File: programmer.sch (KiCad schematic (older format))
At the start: 59 parts, among them U15 93LCxxBT-I_OT, U16 FT2232H, U17 SN74LVC1G32DBVR, U18 SN74LVC2T45DCUR, U19 SN74LVC2T45DCUR, U20 SN74AXC4T245PWR, U21 SN74LVC2T45DCUR, U22 SN74LVC2T45DCUR, U23 SN74LVC2G07DCKR, U24 W25Q64JV, Y2 ECS-3225S33-120-FN-TR

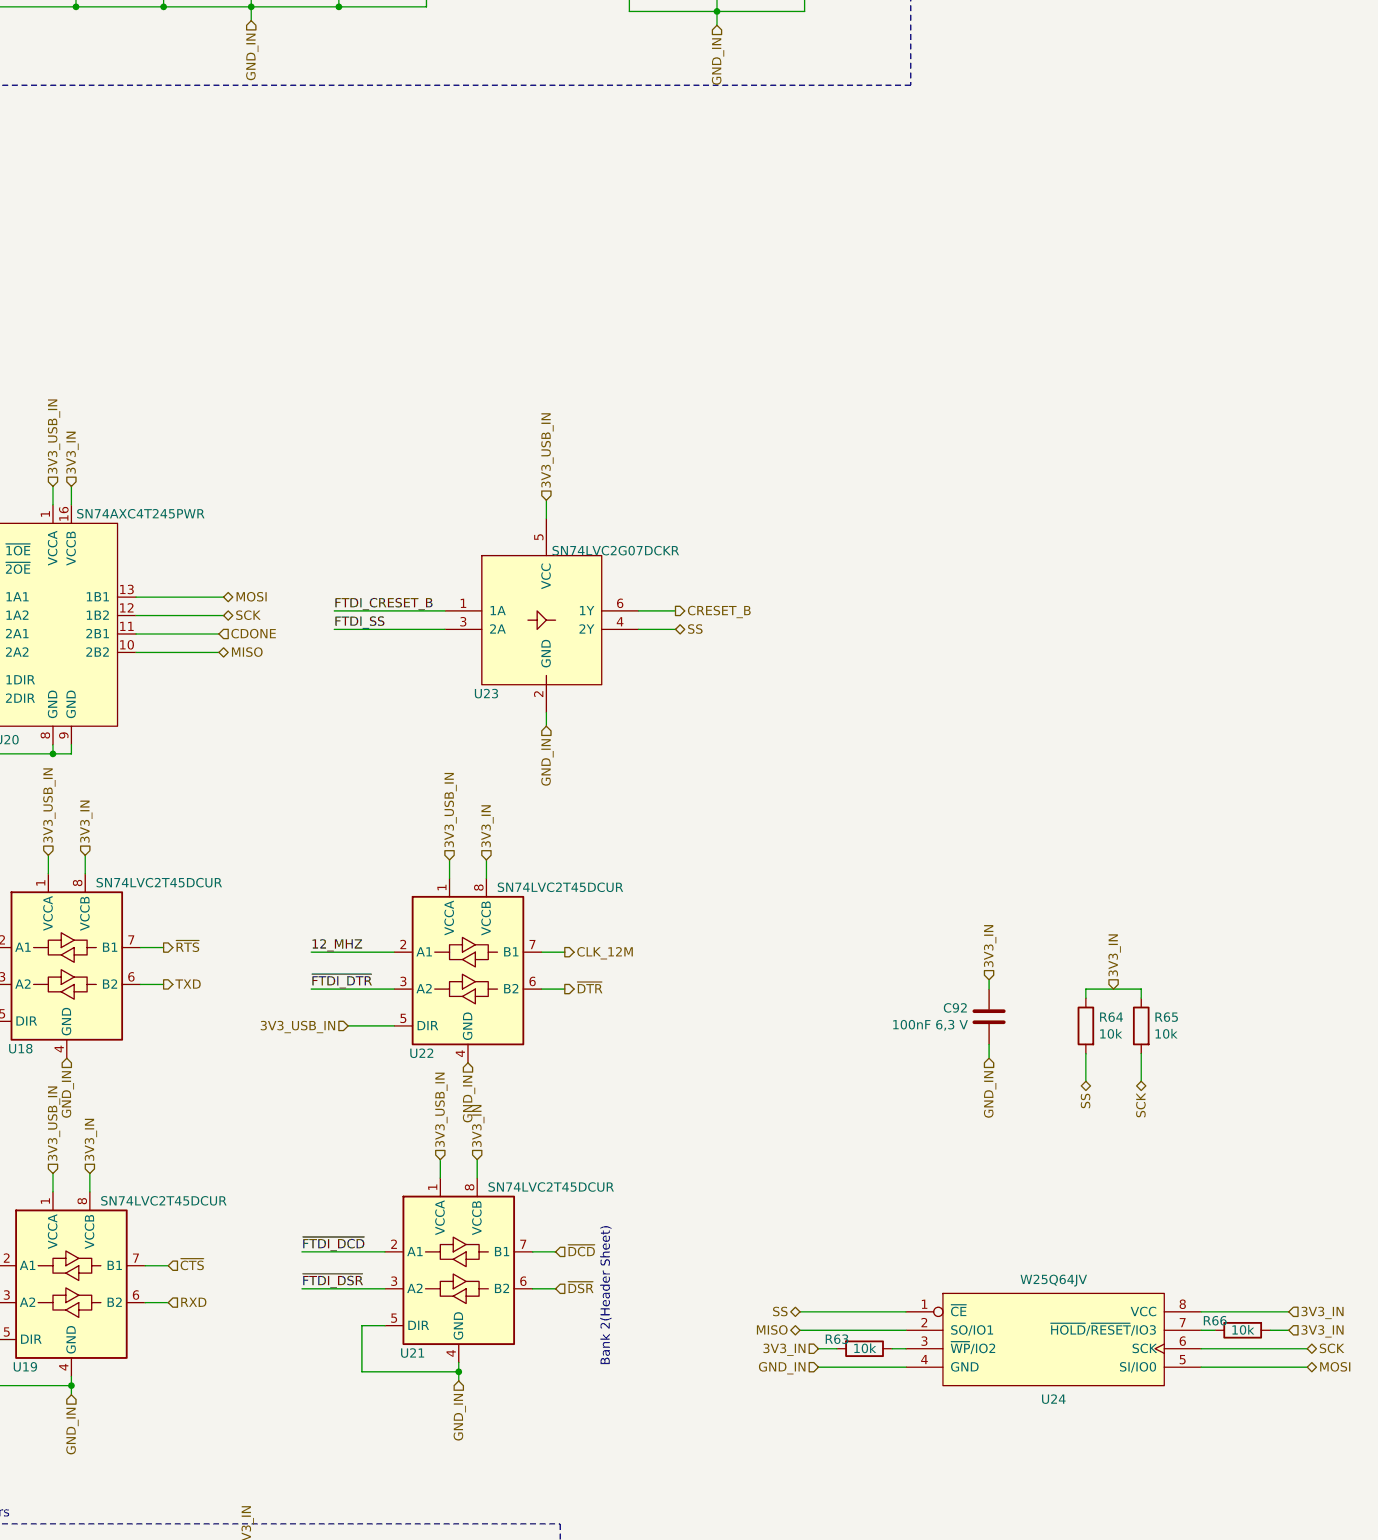
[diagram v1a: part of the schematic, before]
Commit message: Added wires for quad-SPI Flash operation
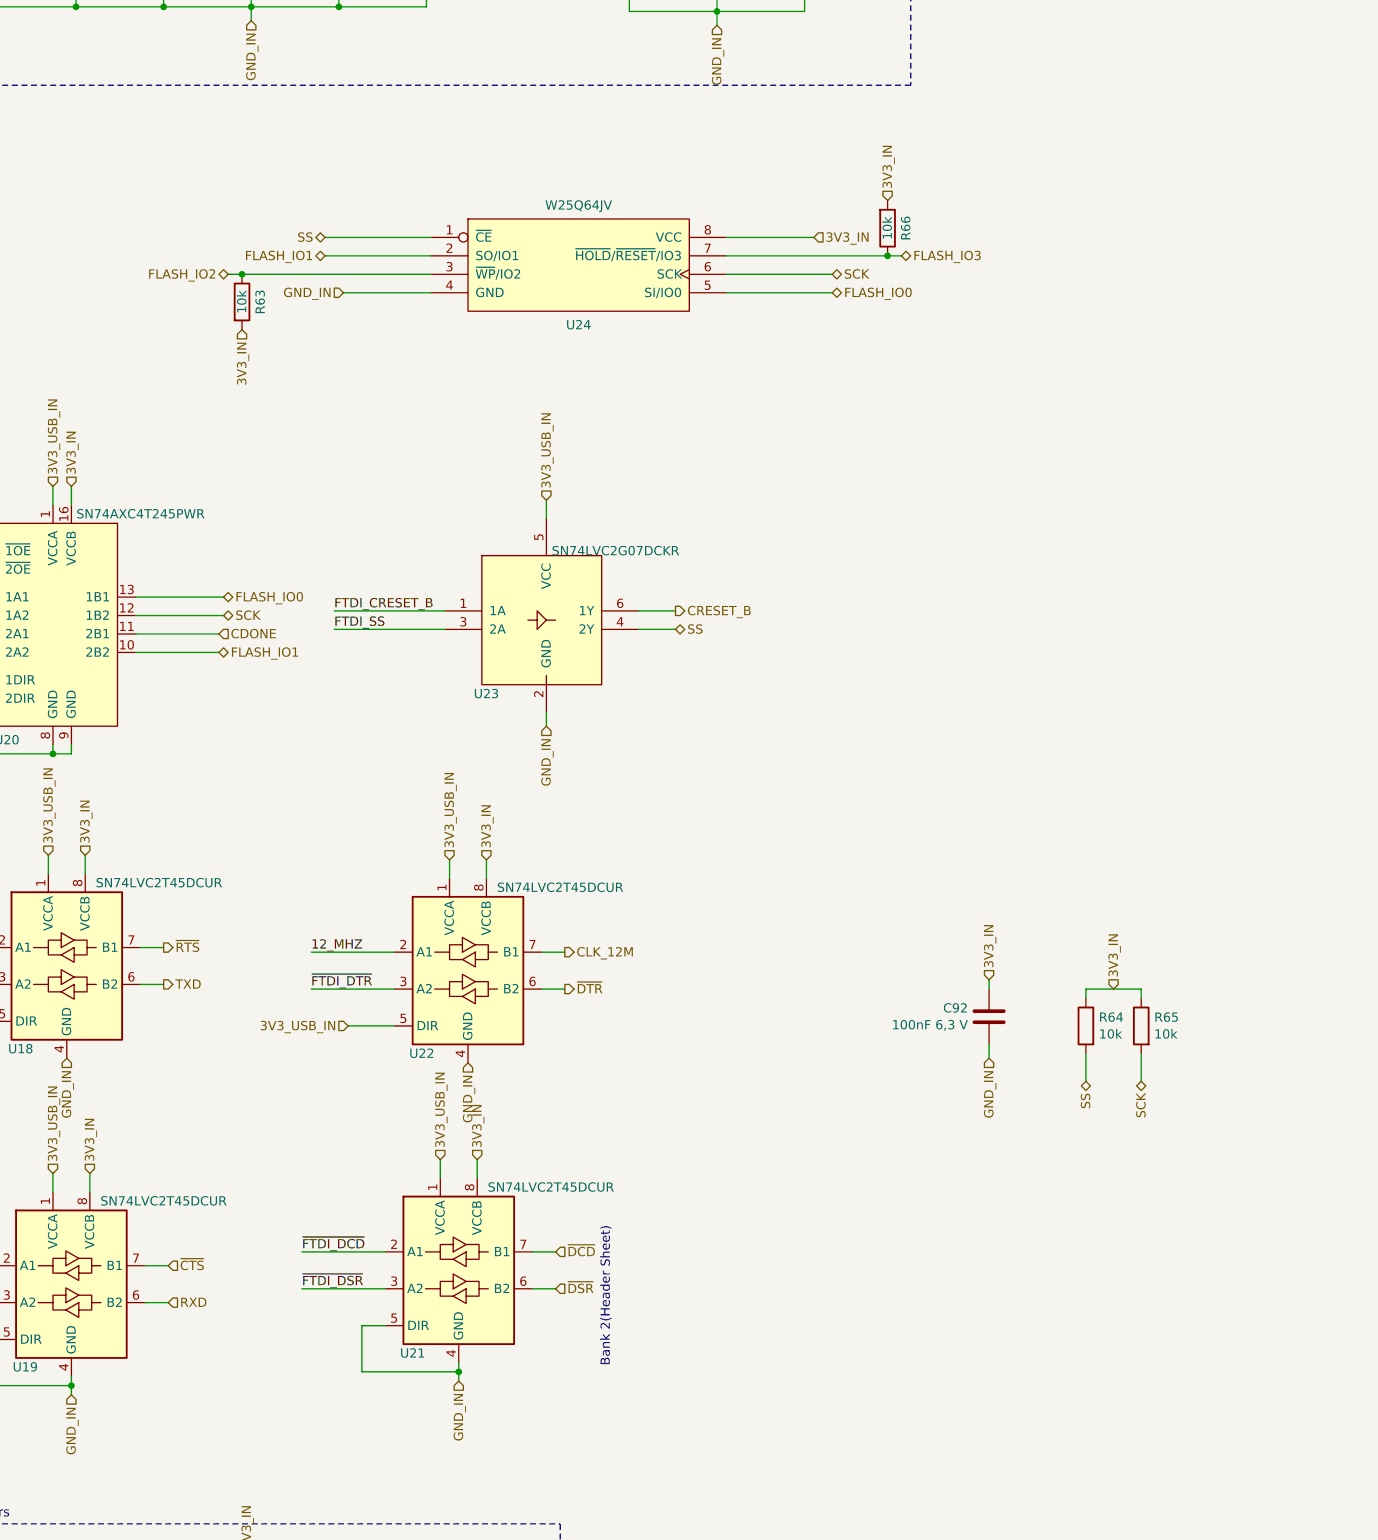
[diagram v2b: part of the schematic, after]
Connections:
- net FLASH_IO3: now reaches R66.1, U24.7 (~HOLD~/~RESET~/IO3)
- net FLASH_IO2: now reaches R63.1, U24.3 (~WP~/IO2)
- net MISO renamed FLASH_IO1
- net MOSI renamed FLASH_IO0
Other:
- moved on the sheet: R63, R66, U24
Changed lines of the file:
@@
 $EndComp
 Wire Wire Line
-	12700 8725 13275 8725
-Wire Wire Line
-	15450 9025 14875 9025
-Wire Wire Line
-	12700 8825 13275 8825
-Wire Wire Line
-	15450 8925 14875 8925
+	10125 2900 10700 2900
+Wire Wire Line
+	12875 3200 12300 3200
+Wire Wire Line
+	10125 3000 10700 3000
+Wire Wire Line
+	12875 3100 12300 3100
 Wire Wire Line
 	5025 4425 5025 4350
@@
 	3125 7625 3175 7625
 Wire Wire Line
-	15350 8725 14875 8725
-Wire Wire Line
-	12800 9025 13275 9025
+	12775 2900 12300 2900
+Wire Wire Line
+	10225 3200 10700 3200
 Wire Wire Line
 	4625 4425 4625 4350
@@
 	9575 4950 9100 4950
 $Comp
-L Device:R R66
-U 1 1 5CD40B26
-P 15100 8825
-F 0 "R66" V 15050 8975 50  0000 C CNN
-F 1 "10k" V 15100 8825 50  0000 C CNN
-F 2 "Resistor_SMD:R_0603_1608Metric" V 15030 8825 50  0001 C CNN
-F 3 "~" H 15100 8825 50  0001 C CNN
-F 4 "RES 10K OHM 5% 1/10W 0603" H 0   700 50  0001 C CNN "Description"
-F 5 "RMCF0603JT10K0CT-ND" H 0   700 50  0001 C CNN "Digikey"
-F 6 "Stackpole Electronics Inc" H 0   700 50  0001 C CNN "Mfg Name"
-F 7 "RMCF0603JT10K0" H 0   700 50  0001 C CNN "Mfg Part Num"
-F 8 "Any" H 0   700 50  0001 C CNN "Spec"
-	1    15100 8825
-	0    -1   1    0
-$EndComp
-Wire Wire Line
-	14875 8825 14950 8825
-Wire Wire Line
-	15350 8825 15250 8825
-$Comp
 L Device:R R63
 U 1 1 5CD829A8
-P 13050 8925
-F 0 "R63" V 13000 8775 50  0000 C CNN
-F 1 "10k" V 13050 8925 50  0000 C CNN
-F 2 "Resistor_SMD:R_0603_1608Metric" V 12980 8925 50  0001 C CNN
-F 3 "~" H 13050 8925 50  0001 C CNN
-F 4 "RES 10K OHM 5% 1/10W 0603" H 0   700 50  0001 C CNN "Description"
-F 5 "RMCF0603JT10K0CT-ND" H 0   700 50  0001 C CNN "Digikey"
-F 6 "Stackpole Electronics Inc" H 0   700 50  0001 C CNN "Mfg Name"
-F 7 "RMCF0603JT10K0" H 0   700 50  0001 C CNN "Mfg Part Num"
-F 8 "Any" H 0   700 50  0001 C CNN "Spec"
-	1    13050 8925
-	0    1    1    0
-$EndComp
-Wire Wire Line
-	13275 8925 13200 8925
-Wire Wire Line
-	12800 8925 12900 8925
+P 9675 3250
+F 0 "R63" V 9775 3250 50  0000 C CNN
+F 1 "10k" V 9675 3250 50  0000 C CNN
+F 2 "Resistor_SMD:R_0603_1608Metric" V 9605 3250 50  0001 C CNN
+F 3 "~" H 9675 3250 50  0001 C CNN
+F 4 "RES 10K OHM 5% 1/10W 0603" H -3375 -4975 50  0001 C CNN "Description"
+F 5 "RMCF0603JT10K0CT-ND" H -3375 -4975 50  0001 C CNN "Digikey"
+F 6 "Stackpole Electronics Inc" H -3375 -4975 50  0001 C CNN "Mfg Name"
+F 7 "RMCF0603JT10K0" H -3375 -4975 50  0001 C CNN "Mfg Part Num"
+F 8 "Any" H -3375 -4975 50  0001 C CNN "Spec"
+	1    9675 3250
+	1    0    0    -1
+$EndComp
 $Comp
 L Device:R R64
@@
 Text HLabel 14400 6975 1    50   Input ~ 0
 3V3_IN
-Text HLabel 15350 8725 2    50   Input ~ 0
+Text HLabel 12775 2900 2    50   Input ~ 0
 3V3_IN
-Text HLabel 15350 8825 2    50   Input ~ 0
+Text HLabel 13175 2700 1    50   Input ~ 0
 3V3_IN
-Text HLabel 12800 8925 0    50   Input ~ 0
+Text HLabel 9675 3400 3    50   Input ~ 0
 3V3_IN
-Text HLabel 12800 9025 0    50   Input ~ 0
+Text HLabel 10225 3200 0    50   Input ~ 0
 GND_IN
 Text HLabel 13725 7350 3    50   Input ~ 0
@@
 RXD
 Text HLabel 9575 4850 2    50   BiDi ~ 0
-MOSI
+FLASH_IO0
 Text HLabel 9575 4950 2    50   BiDi ~ 0
 SCK
@@
 CDONE
 Text HLabel 9550 5150 2    50   BiDi ~ 0
-MISO
+FLASH_IO1
 Text HLabel 12025 5025 2    50   BiDi ~ 0
 SS
@@
 Text HLabel 11375 8600 2    50   Input ~ 0
 ~DSR~
-Text HLabel 12700 8725 0    50   BiDi ~ 0
+Text HLabel 10125 2900 0    50   BiDi ~ 0
 SS
-Text HLabel 12700 8825 0    50   BiDi ~ 0
-MISO
-Text HLabel 15450 8925 2    50   BiDi ~ 0
+Text HLabel 10125 3000 0    50   BiDi ~ 0
+FLASH_IO1
+Text HLabel 12875 3100 2    50   BiDi ~ 0
 SCK
-Text HLabel 15450 9025 2    50   BiDi ~ 0
-MOSI
+Text HLabel 12875 3200 2    50   BiDi ~ 0
+FLASH_IO0
 Text HLabel 14250 7475 3    50   BiDi ~ 0
 SS
@@
 L W25Q64JV:W25Q64JV U24
 U 1 1 5EED1082
-P 14075 8875
-F 0 "U24" H 14075 8550 50  0000 C CNN
-F 1 "W25Q64JV" H 14075 9199 50  0000 C CNN
-F 2 "Package_SO:SOIC-8_5.23x5.23mm_P1.27mm" H 14075 8475 50  0001 C CNN
-F 3 "https://www.winbond.com/resource-files/w25q64jv%20revj%2003272018%20plus.pdf" H 14075 8475 50  0001 C CNN
-F 4 "IC FLASH 64M SPI 133MHZ 8SOIC" H 14075 8875 50  0001 C CNN "Description"
-F 5 "W25Q64JVSSIMCT-ND" H 14075 8875 50  0001 C CNN "Digikey"
-F 6 "Winbond Electronics" H 14075 8875 50  0001 C CNN "Mfg Name"
-F 7 "W25Q64JVSSIM TR" H 14075 8875 50  0001 C CNN "Mfg Part Num"
-F 8 "Spec" H 14075 8875 50  0001 C CNN "Spec"
-	1    14075 8875
-	1    0    0    -1
-$EndComp
+P 11500 3050
+F 0 "U24" H 11500 2725 50  0000 C CNN
+F 1 "W25Q64JV" H 11500 3374 50  0000 C CNN
+F 2 "Package_SO:SOIC-8_5.23x5.23mm_P1.27mm" H 11500 2650 50  0001 C CNN
+F 3 "https://www.winbond.com/resource-files/w25q64jv%20revj%2003272018%20plus.pdf" H 11500 2650 50  0001 C CNN
+F 4 "IC FLASH 64M SPI 133MHZ 8SOIC" H 11500 3050 50  0001 C CNN "Description"
+F 5 "W25Q64JVSSIMCT-ND" H 11500 3050 50  0001 C CNN "Digikey"
+F 6 "Winbond Electronics" H 11500 3050 50  0001 C CNN "Mfg Name"
+F 7 "W25Q64JVSSIM TR" H 11500 3050 50  0001 C CNN "Mfg Part Num"
+F 8 "Spec" H 11500 3050 50  0001 C CNN "Spec"
+	1    11500 3050
+	1    0    0    -1
+$EndComp
+$Comp
+L Device:R R66
+U 1 1 5CD40B26
+P 13175 2850
+F 0 "R66" V 13275 2850 50  0000 C CNN
+F 1 "10k" V 13175 2850 50  0000 C CNN
+F 2 "Resistor_SMD:R_0603_1608Metric" V 13105 2850 50  0001 C CNN
+F 3 "~" H 13175 2850 50  0001 C CNN
+F 4 "RES 10K OHM 5% 1/10W 0603" H -1925 -5275 50  0001 C CNN "Description"
+F 5 "RMCF0603JT10K0CT-ND" H -1925 -5275 50  0001 C CNN "Digikey"
+F 6 "Stackpole Electronics Inc" H -1925 -5275 50  0001 C CNN "Mfg Name"
+F 7 "RMCF0603JT10K0" H -1925 -5275 50  0001 C CNN "Mfg Part Num"
+F 8 "Any" H -1925 -5275 50  0001 C CNN "Spec"
+	1    13175 2850
+	1    0    0    1
+$EndComp
+Text HLabel 13250 3000 2    50   BiDi ~ 0
+FLASH_IO3
+Text HLabel 9600 3100 0    50   BiDi ~ 0
+FLASH_IO2
+Wire Wire Line
+	13250 3000 13175 3000
+Wire Wire Line
+	9600 3100 9675 3100
+Connection ~ 9675 3100
+Wire Wire Line
+	9675 3100 10700 3100
+Connection ~ 13175 3000
+Wire Wire Line
+	13175 3000 12300 3000
 $EndSCHEMATC

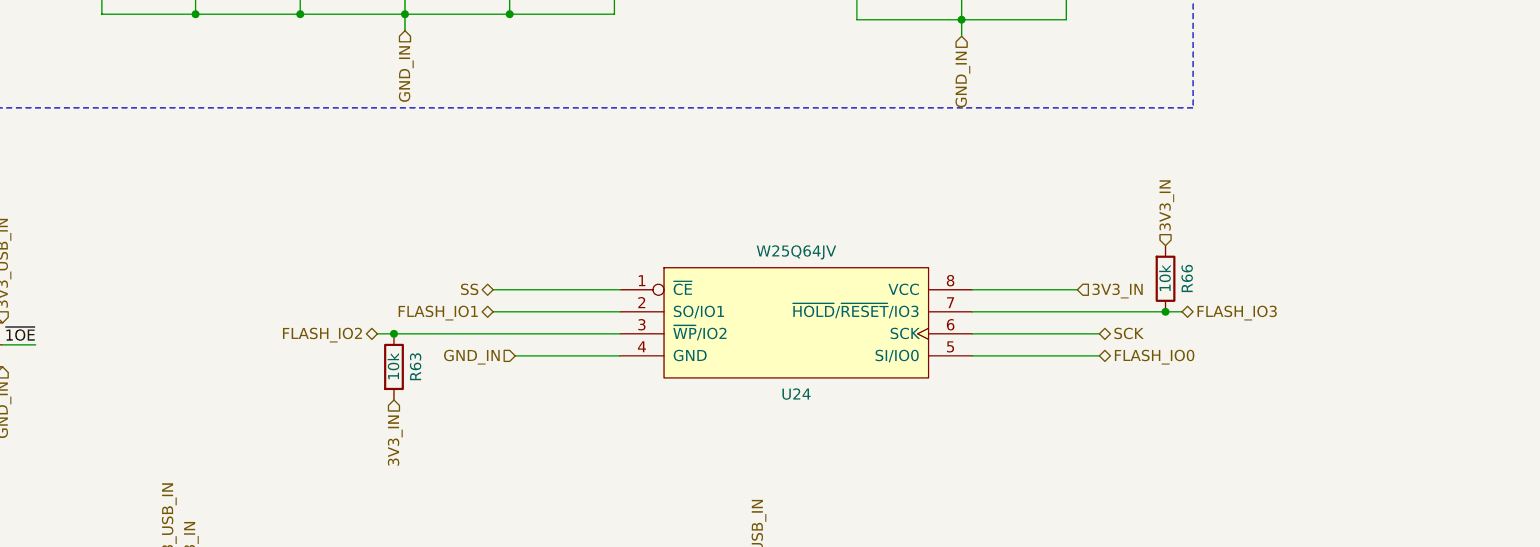
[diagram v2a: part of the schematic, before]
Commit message: 7-17 VIN Power PIN Header moved to the left for better compatibility with extension boards. Added 0 Ohm resistors for optional desoldering of quad-SPI wires. USB power jumper moved more to the side of the board. Arduino Header decoupling capacitors moved to arduino header sheet.
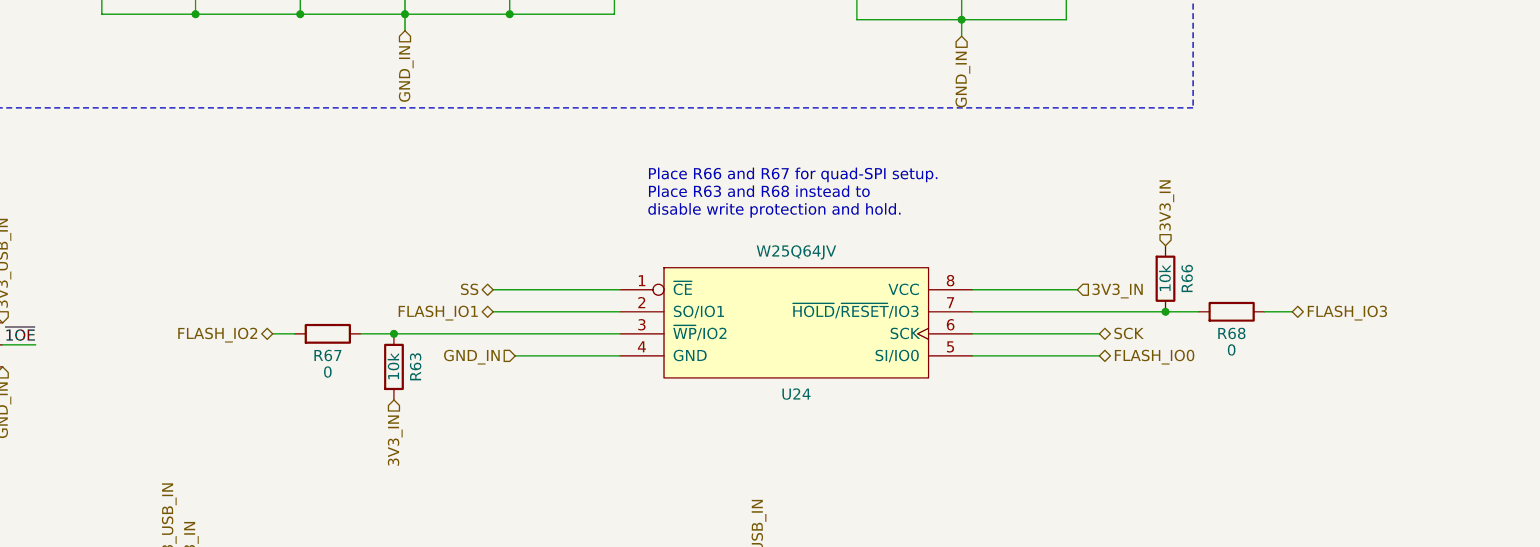
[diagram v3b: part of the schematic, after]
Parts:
- added R67, R68: 0, Resistor_SMD:R_0603_1608Metric, symbol Device:R
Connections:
- net FLASH_IO2: now also R67.2; no longer R63.1, U24.3 (~WP~/IO2)
- net FLASH_IO3: now also R68.1; no longer R66.1, U24.7 (~HOLD~/~RESET~/IO3)
- new net: R66.1, R68.2, U24.7 (~HOLD~/~RESET~/IO3)
- new net: R63.1, R67.1, U24.3 (~WP~/IO2)
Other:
- note added: "Place R66 and R67 for quad-SPI setup. \nPlace R63 and R68 instead to \ndisable write protection and hold."
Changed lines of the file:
@@
 	1    0    0    1
 $EndComp
-Text HLabel 13250 3000 2    50   BiDi ~ 0
+Text HLabel 13750 3000 2    50   BiDi ~ 0
 FLASH_IO3
-Text HLabel 9600 3100 0    50   BiDi ~ 0
+Text HLabel 9125 3100 0    50   BiDi ~ 0
 FLASH_IO2
 Wire Wire Line
-	13250 3000 13175 3000
+	9675 3100 10700 3100
 Wire Wire Line
-	9600 3100 9675 3100
+	13175 3000 12300 3000
+$Comp
+L Device:R R?
+U 1 1 5F23BC79
+P 9375 3100
+AR Path="/5CAB7CD4/5F23BC79" Ref="R?"  Part="1"
+AR Path="/5CB5889B/5F23BC79" Ref="R?"  Part="1"
+AR Path="/5ED96D61/5F23BC79" Ref="R?"  Part="1"
+AR Path="/5ED0B946/5F23BC79" Ref="R67"  Part="1"
+F 0 "R67" V 9275 3100 50  0000 C CNN
+F 1 "0" V 9200 3100 50  0000 C CNN
+F 2 "Resistor_SMD:R_0603_1608Metric" V 9305 3100 50  0001 C CNN
+F 3 "~" H 9375 3100 50  0001 C CNN
+F 4 "" V 9490 3100 50  0000 C CNN "DNP"
+	1    9375 3100
+	0    1    -1   0
+$EndComp
+$Comp
+L Device:R R?
+U 1 1 5F254C66
+P 13475 3000
+AR Path="/5CAB7CD4/5F254C66" Ref="R?"  Part="1"
+AR Path="/5CB5889B/5F254C66" Ref="R?"  Part="1"
+AR Path="/5ED96D61/5F254C66" Ref="R?"  Part="1"
+AR Path="/5ED0B946/5F254C66" Ref="R68"  Part="1"
+F 0 "R68" V 13375 3000 50  0000 C CNN
+F 1 "0" V 13300 3000 50  0000 C CNN
+F 2 "Resistor_SMD:R_0603_1608Metric" V 13405 3000 50  0001 C CNN
+F 3 "~" H 13475 3000 50  0001 C CNN
+F 4 "" V 13590 3000 50  0000 C CNN "DNP"
+	1    13475 3000
+	0    1    -1   0
+$EndComp
+Wire Wire Line
+	13175 3000 13325 3000
+Connection ~ 13175 3000
+Wire Wire Line
+	13625 3000 13750 3000
+Wire Wire Line
+	9675 3100 9525 3100
 Connection ~ 9675 3100
 Wire Wire Line
-	9675 3100 10700 3100
-Connection ~ 13175 3000
-Wire Wire Line
-	13175 3000 12300 3000
+	9225 3100 9125 3100
+Text Notes 10825 2575 0    50   ~ 0
+Place R66 and R67 for quad-SPI setup. \nPlace R63 and R68 instead to \ndisable write protection and hold.
 $EndSCHEMATC
